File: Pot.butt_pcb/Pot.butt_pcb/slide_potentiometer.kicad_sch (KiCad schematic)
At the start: 16 parts

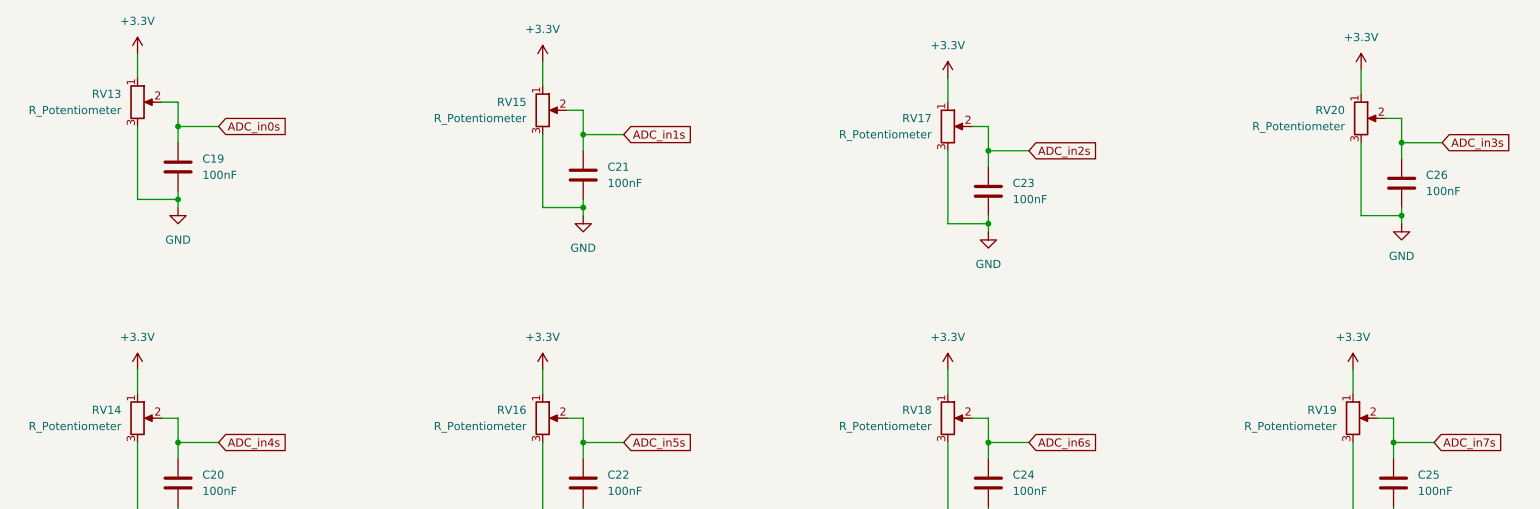
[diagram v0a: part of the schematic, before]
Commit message: fixing keyboard and pot project schematics
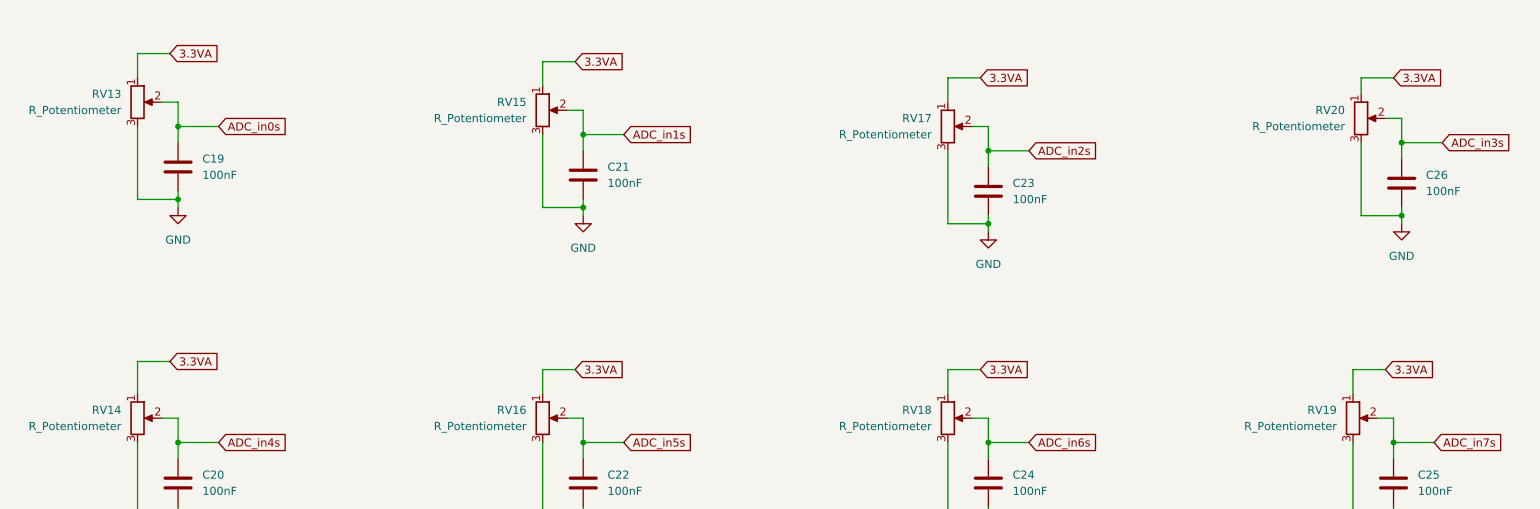
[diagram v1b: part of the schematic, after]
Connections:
- net +3V3 renamed 3.3VA

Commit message: main_func pcb done
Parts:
- RV13, RV14, RV15, RV16, RV17, RV18, RV19, RV20: footprint (none) -> Connector_PinSocket_2.54mm:PinSocket_1x03_P2.54mm_Horizontal
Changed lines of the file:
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@@
       (effects (font (size 1.27 1.27)) (justify right))
     )
-    (property "Footprint" "" (id 2) (at 243.84 46.99 0)
+    (property "Footprint" "Connector_PinSocket_2.54mm:PinSocket_1x03_P2.54mm_Horizontal" (id 2) (at 243.84 46.99 0)
       (effects (font (size 1.27 1.27)) hide)
     )
@@
       (effects (font (size 1.27 1.27)) (justify right))
     )
-    (property "Footprint" "" (id 2) (at 179.07 48.26 0)
+    (property "Footprint" "Connector_PinSocket_2.54mm:PinSocket_1x03_P2.54mm_Horizontal" (id 2) (at 179.07 48.26 0)
       (effects (font (size 1.27 1.27)) hide)
     )
@@
       (effects (font (size 1.27 1.27)) (justify right))
     )
-    (property "Footprint" "" (id 2) (at 52.07 44.45 0)
+    (property "Footprint" "Connector_PinSocket_2.54mm:PinSocket_1x03_P2.54mm_Horizontal" (id 2) (at 52.07 44.45 0)
       (effects (font (size 1.27 1.27)) hide)
     )
@@
       (effects (font (size 1.27 1.27)) (justify right))
     )
-    (property "Footprint" "" (id 2) (at 242.57 93.98 0)
+    (property "Footprint" "Connector_PinSocket_2.54mm:PinSocket_1x03_P2.54mm_Horizontal" (id 2) (at 242.57 93.98 0)
       (effects (font (size 1.27 1.27)) hide)
     )
@@
       (effects (font (size 1.27 1.27)) (justify right))
     )
-    (property "Footprint" "" (id 2) (at 179.07 93.98 0)
+    (property "Footprint" "Connector_PinSocket_2.54mm:PinSocket_1x03_P2.54mm_Horizontal" (id 2) (at 179.07 93.98 0)
       (effects (font (size 1.27 1.27)) hide)
     )
@@
       (effects (font (size 1.27 1.27)) (justify right))
     )
-    (property "Footprint" "" (id 2) (at 115.57 45.72 0)
+    (property "Footprint" "Connector_PinSocket_2.54mm:PinSocket_1x03_P2.54mm_Horizontal" (id 2) (at 115.57 45.72 0)
       (effects (font (size 1.27 1.27)) hide)
     )
@@
       (effects (font (size 1.27 1.27)) (justify right))
     )
-    (property "Footprint" "" (id 2) (at 115.57 93.98 0)
+    (property "Footprint" "Connector_PinSocket_2.54mm:PinSocket_1x03_P2.54mm_Horizontal" (id 2) (at 115.57 93.98 0)
       (effects (font (size 1.27 1.27)) hide)
     )
@@
       (effects (font (size 1.27 1.27)) (justify right))
     )
-    (property "Footprint" "" (id 2) (at 52.07 93.98 0)
-      (effects (font (size 1.27 1.27)) hide)
-    )
+    (property "Footprint" "Connector_PinSocket_2.54mm:PinSocket_1x03_P2.54mm_Horizontal" (id 2) (at 52.07 93.98 0)
+      (effects (font (size 1.27 1.27)) hide)
+    )

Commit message: Pot.but_pcb in progress
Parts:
- RV13, RV14, RV15, RV16, RV17, RV18, RV19, RV20: footprint Connector_PinSocket_2.54mm:PinSocket_1x03_P2.54mm_Horizontal -> Connector_PinSocket_2.54mm:PinSocket_1x03_P2.54mm_Vertical
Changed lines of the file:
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@@
       (effects (font (size 1.27 1.27)) (justify right))
     )
-    (property "Footprint" "Connector_PinSocket_2.54mm:PinSocket_1x03_P2.54mm_Horizontal" (id 2) (at 243.84 46.99 0)
+    (property "Footprint" "Connector_PinSocket_2.54mm:PinSocket_1x03_P2.54mm_Vertical" (id 2) (at 243.84 46.99 0)
       (effects (font (size 1.27 1.27)) hide)
     )
@@
       (effects (font (size 1.27 1.27)) (justify right))
     )
-    (property "Footprint" "Connector_PinSocket_2.54mm:PinSocket_1x03_P2.54mm_Horizontal" (id 2) (at 179.07 48.26 0)
+    (property "Footprint" "Connector_PinSocket_2.54mm:PinSocket_1x03_P2.54mm_Vertical" (id 2) (at 179.07 48.26 0)
       (effects (font (size 1.27 1.27)) hide)
     )
@@
       (effects (font (size 1.27 1.27)) (justify right))
     )
-    (property "Footprint" "Connector_PinSocket_2.54mm:PinSocket_1x03_P2.54mm_Horizontal" (id 2) (at 52.07 44.45 0)
+    (property "Footprint" "Connector_PinSocket_2.54mm:PinSocket_1x03_P2.54mm_Vertical" (id 2) (at 52.07 44.45 0)
       (effects (font (size 1.27 1.27)) hide)
     )
@@
       (effects (font (size 1.27 1.27)) (justify right))
     )
-    (property "Footprint" "Connector_PinSocket_2.54mm:PinSocket_1x03_P2.54mm_Horizontal" (id 2) (at 242.57 93.98 0)
+    (property "Footprint" "Connector_PinSocket_2.54mm:PinSocket_1x03_P2.54mm_Vertical" (id 2) (at 242.57 93.98 0)
       (effects (font (size 1.27 1.27)) hide)
     )
@@
       (effects (font (size 1.27 1.27)) (justify right))
     )
-    (property "Footprint" "Connector_PinSocket_2.54mm:PinSocket_1x03_P2.54mm_Horizontal" (id 2) (at 179.07 93.98 0)
+    (property "Footprint" "Connector_PinSocket_2.54mm:PinSocket_1x03_P2.54mm_Vertical" (id 2) (at 179.07 93.98 0)
       (effects (font (size 1.27 1.27)) hide)
     )
@@
       (effects (font (size 1.27 1.27)) (justify right))
     )
-    (property "Footprint" "Connector_PinSocket_2.54mm:PinSocket_1x03_P2.54mm_Horizontal" (id 2) (at 115.57 45.72 0)
+    (property "Footprint" "Connector_PinSocket_2.54mm:PinSocket_1x03_P2.54mm_Vertical" (id 2) (at 115.57 45.72 0)
       (effects (font (size 1.27 1.27)) hide)
     )
@@
       (effects (font (size 1.27 1.27)) (justify right))
     )
-    (property "Footprint" "Connector_PinSocket_2.54mm:PinSocket_1x03_P2.54mm_Horizontal" (id 2) (at 115.57 93.98 0)
+    (property "Footprint" "Connector_PinSocket_2.54mm:PinSocket_1x03_P2.54mm_Vertical" (id 2) (at 115.57 93.98 0)
       (effects (font (size 1.27 1.27)) hide)
     )
@@
       (effects (font (size 1.27 1.27)) (justify right))
     )
-    (property "Footprint" "Connector_PinSocket_2.54mm:PinSocket_1x03_P2.54mm_Horizontal" (id 2) (at 52.07 93.98 0)
-      (effects (font (size 1.27 1.27)) hide)
-    )
+    (property "Footprint" "Connector_PinSocket_2.54mm:PinSocket_1x03_P2.54mm_Vertical" (id 2) (at 52.07 93.98 0)
+      (effects (font (size 1.27 1.27)) hide)
+    )

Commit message: pcb design fixing
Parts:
- removed RV13, RV14, RV15, RV16, RV17, RV18, RV19, RV20: R_Potentiometer, Connector_PinSocket_2.54mm:PinSocket_1x03_P2.54mm_Vertical, symbol Device:R_Potentiometer
- added C10, C11, C12, C13, C14, C3, C4, C5, C6, C7, C8, C9: 100nF, Capacitor_SMD:C_0805_2012Metric_Pad1.18x1.45mm_HandSolder, symbol Device:C
- added J4, J5, J6: Conn_01x40_Male, Connector_IDC:IDC-Header_2x20_P2.54mm_Vertical, symbol Connector:Conn_01x40_Male
- added R27, R28, R29, R4, R5, R6, R7, R8: 100, Resistor_SMD:R_0805_2012Metric_Pad1.20x1.40mm_HandSolder, symbol Device:R
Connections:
- net 3.3VA: now also J4.10 (Pin_10), J4.14 (Pin_14), J4.18 (Pin_18), J4.2 (Pin_2), J4.22 (Pin_22), J4.26 (Pin_26), J4.30 (Pin_30), J4.34 (Pin_34), J4.38 (Pin_38), J4.6 (Pin_6), J5.10 (Pin_10), J5.14 (Pin_14), J5.18 (Pin_18), J5.2 (Pin_2), J5.22 (Pin_22), J5.26 (Pin_26), J5.30 (Pin_30), J5.34 (Pin_34), J5.38 (Pin_38), J5.6 (Pin_6)
- net ADC_in0s: now also J4.4 (Pin_4)
- net ADC_in1s: now also J4.8 (Pin_8)
- net ADC_in2s: now also J4.12 (Pin_12)
- net ADC_in3s: now also J4.16 (Pin_16)
- net ADC_in4s: now also J4.20 (Pin_20)
- net ADC_in5s: now also J4.24 (Pin_24)
- net ADC_in6s: now also J4.28 (Pin_28)
- net ADC_in7s: now also J4.32 (Pin_32)
- net GND: now also C10.2, C11.2, C12.2, C13.2, C14.2, C3.2, C4.2, C5.2, C6.2, C7.2, C8.2, C9.2, J4.1 (Pin_1), J4.11 (Pin_11), J4.13 (Pin_13), J4.15 (Pin_15), J4.17 (Pin_17), J4.19 (Pin_19), J4.21 (Pin_21), J4.23 (Pin_23), J4.25 (Pin_25), J4.27 (Pin_27), J4.29 (Pin_29), J4.3 (Pin_3), J4.31 (Pin_31), J4.33 (Pin_33), J4.35 (Pin_35), J4.37 (Pin_37), J4.39 (Pin_39), J4.5 (Pin_5), J4.7 (Pin_7), J4.9 (Pin_9), J5.1 (Pin_1), J5.11 (Pin_11), J5.13 (Pin_13), J5.15 (Pin_15), J5.17 (Pin_17), J5.19 (Pin_19), J5.21 (Pin_21), J5.23 (Pin_23), J5.25 (Pin_25), J5.27 (Pin_27), J5.29 (Pin_29), J5.3 (Pin_3), J5.31 (Pin_31), J5.33 (Pin_33), J5.35 (Pin_35), J5.37 (Pin_37), J5.39 (Pin_39), J5.5 (Pin_5), J5.7 (Pin_7), J5.9 (Pin_9), J6.1 (Pin_1), J6.11 (Pin_11), J6.13 (Pin_13), J6.15 (Pin_15), J6.17 (Pin_17), J6.19 (Pin_19), J6.21 (Pin_21), J6.23 (Pin_23), J6.25 (Pin_25), J6.27 (Pin_27), J6.29 (Pin_29), J6.3 (Pin_3), J6.31 (Pin_31), J6.33 (Pin_33), J6.34 (Pin_34), J6.35 (Pin_35), J6.36 (Pin_36), J6.37 (Pin_37), J6.38 (Pin_38), J6.39 (Pin_39), J6.40 (Pin_40), J6.5 (Pin_5), J6.7 (Pin_7), J6.9 (Pin_9)
- new net +3V3: J6.10 (Pin_10), J6.14 (Pin_14), J6.18 (Pin_18), J6.2 (Pin_2), J6.22 (Pin_22), J6.26 (Pin_26), J6.30 (Pin_30), J6.6 (Pin_6)
- new net ADC_in0p: C3.1, J4.36 (Pin_36)
- new net ADC_in10p: C11.1, J5.36 (Pin_36)
- new net ADC_in11p: C14.1, J5.40 (Pin_40)
- new net ADC_in1p: C6.1, J4.40 (Pin_40)
- new net ADC_in2p: C9.1, J5.4 (Pin_4)
- new net ADC_in3p: C12.1, J5.8 (Pin_8)
- new net ADC_in4p: C4.1, J5.12 (Pin_12)
- new net ADC_in5p: C7.1, J5.16 (Pin_16)
- new net ADC_in6p: C10.1, J5.20 (Pin_20)
- new net ADC_in7p: C13.1, J5.24 (Pin_24)
- new net ADC_in8p: C5.1, J5.28 (Pin_28)
- new net ADC_in9p: C8.1, J5.32 (Pin_32)
- new net SW1: J6.4 (Pin_4), R4.2
- new net SW1p: R4.1
- new net SW2: J6.8 (Pin_8), R6.2
- new net SW2p: R6.1
- new net SW3: J6.12 (Pin_12), R8.2
- new net SW3p: R8.1
- new net SW4: J6.16 (Pin_16), R28.2
- new net SW4p: R28.1
- new net SW5: J6.20 (Pin_20), R5.2
- new net SW5p: R5.1
- new net SW6: J6.24 (Pin_24), R7.2
- new net SW6p: R7.1
- new net SW7: J6.28 (Pin_28), R27.2
- new net SW7p: R27.1
- new net SW8: J6.32 (Pin_32), R29.2
- new net SW8p: R29.1
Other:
- moved on the sheet: C19, C20, C21, C22, C23, C24, C25, C26

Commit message: gerber files generated
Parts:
- added H1, H2, H3, H4, H5, H6: MountingHole, MountingHole:MountingHole_3.2mm_M3_Pad_Via, symbol Mechanical:MountingHole
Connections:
- net +3V3: now also J6.12 (Pin_12), J6.16 (Pin_16), J6.20 (Pin_20), J6.24 (Pin_24), J6.28 (Pin_28), J6.32 (Pin_32), J6.36 (Pin_36), J6.40 (Pin_40); no longer J6.10 (Pin_10), J6.14 (Pin_14), J6.18 (Pin_18), J6.2 (Pin_2), J6.22 (Pin_22), J6.26 (Pin_26), J6.30 (Pin_30), J6.6 (Pin_6)
- net 3.3VA: now also J4.12 (Pin_12), J4.16 (Pin_16), J4.20 (Pin_20), J4.24 (Pin_24), J4.28 (Pin_28), J4.32 (Pin_32), J4.36 (Pin_36), J4.4 (Pin_4), J4.40 (Pin_40), J4.8 (Pin_8), J5.12 (Pin_12), J5.16 (Pin_16), J5.20 (Pin_20), J5.24 (Pin_24), J5.28 (Pin_28), J5.32 (Pin_32), J5.36 (Pin_36), J5.4 (Pin_4), J5.40 (Pin_40), J5.8 (Pin_8); no longer J4.10 (Pin_10), J4.14 (Pin_14), J4.18 (Pin_18), J4.2 (Pin_2), J4.22 (Pin_22), J4.26 (Pin_26), J4.30 (Pin_30), J4.34 (Pin_34), J4.38 (Pin_38), J4.6 (Pin_6), J5.10 (Pin_10), J5.14 (Pin_14), J5.18 (Pin_18), J5.2 (Pin_2), J5.22 (Pin_22), J5.26 (Pin_26), J5.30 (Pin_30), J5.34 (Pin_34), J5.38 (Pin_38), J5.6 (Pin_6)
- net ADC_in0p: now also J4.6 (Pin_6); no longer J4.36 (Pin_36)
- net ADC_in0s: now also J4.38 (Pin_38); no longer J4.4 (Pin_4)
- net ADC_in10p: now also J5.6 (Pin_6); no longer J5.36 (Pin_36)
- net ADC_in11p: now also J5.2 (Pin_2); no longer J5.40 (Pin_40)
- net ADC_in1p: now also J4.2 (Pin_2); no longer J4.40 (Pin_40)
- net ADC_in1s: now also J4.34 (Pin_34); no longer J4.8 (Pin_8)
- net ADC_in2p: now also J5.38 (Pin_38); no longer J5.4 (Pin_4)
- net ADC_in2s: now also J4.30 (Pin_30); no longer J4.12 (Pin_12)
- net ADC_in3p: now also J5.34 (Pin_34); no longer J5.8 (Pin_8)
- net ADC_in3s: now also J4.26 (Pin_26); no longer J4.16 (Pin_16)
- net ADC_in4p: now also J5.30 (Pin_30); no longer J5.12 (Pin_12)
- net ADC_in4s: now also J4.22 (Pin_22); no longer J4.20 (Pin_20)
- net ADC_in5p: now also J5.26 (Pin_26); no longer J5.16 (Pin_16)
- net ADC_in5s: now also J4.18 (Pin_18); no longer J4.24 (Pin_24)
- net ADC_in6p: now also J5.22 (Pin_22); no longer J5.20 (Pin_20)
- net ADC_in6s: now also J4.14 (Pin_14); no longer J4.28 (Pin_28)
- net ADC_in7p: now also J5.18 (Pin_18); no longer J5.24 (Pin_24)
- net ADC_in7s: now also J4.10 (Pin_10); no longer J4.32 (Pin_32)
- net ADC_in8p: now also J5.14 (Pin_14); no longer J5.28 (Pin_28)
- net ADC_in9p: now also J5.10 (Pin_10); no longer J5.32 (Pin_32)
- net GND: now also J6.2 (Pin_2), J6.4 (Pin_4), J6.6 (Pin_6), J6.8 (Pin_8); no longer J6.34 (Pin_34), J6.36 (Pin_36), J6.38 (Pin_38), J6.40 (Pin_40)
- net SW1: now also J6.38 (Pin_38); no longer J6.4 (Pin_4)
- net SW2: now also J6.34 (Pin_34); no longer J6.8 (Pin_8)
- net SW3: now also J6.30 (Pin_30); no longer J6.12 (Pin_12)
- net SW4: now also J6.26 (Pin_26); no longer J6.16 (Pin_16)
- net SW5: now also J6.22 (Pin_22); no longer J6.20 (Pin_20)
- net SW6: now also J6.18 (Pin_18); no longer J6.24 (Pin_24)
- net SW7: now also J6.14 (Pin_14); no longer J6.28 (Pin_28)
- net SW8: now also J6.10 (Pin_10); no longer J6.32 (Pin_32)
